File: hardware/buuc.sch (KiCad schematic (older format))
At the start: 12 parts, among them P1 USB_OTG, P2 CONN_01X02, Q1 NDS8434, U1 BOOST_REGULATOR, U2 MCP73842-840I/UN

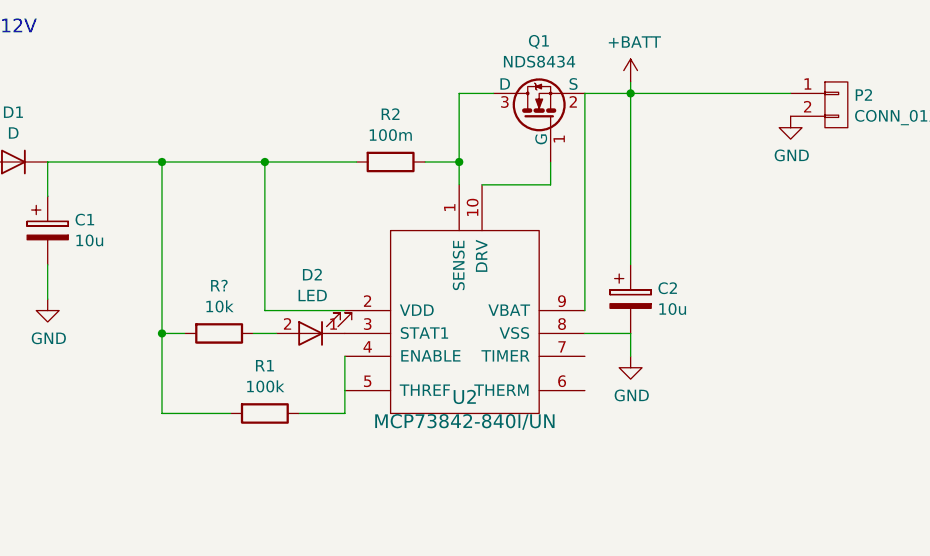
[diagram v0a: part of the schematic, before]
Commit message: Whoops; using the wrong footprint and chip diagram.
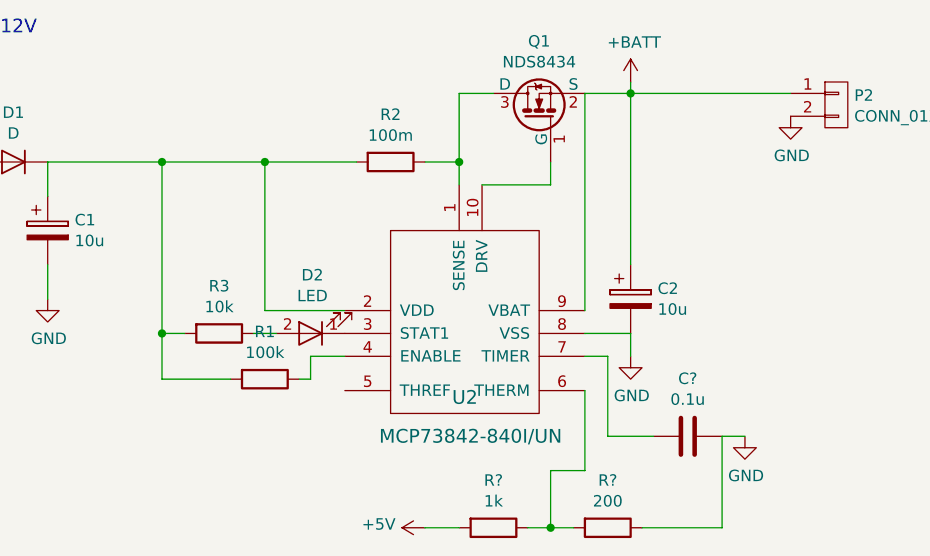
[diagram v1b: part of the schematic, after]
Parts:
- added C?: 0.1u, symbol C
- added R?: 1k, apexelectrix/apex-smd-resistors.pretty:R_0805_HandSoldering, symbol R
- added R?: 200, apexelectrix/apex-smd-resistors.pretty:R_0805_HandSoldering, symbol R
- gave numbers to parts that had none: 1
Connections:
- net +5V: now also R?.2
- net GND: now also C?.1, R?.1
- net at U2.6 (THERM): now also R?.1, R?.2
- net at U2.7 (TIMER): now also C?.2
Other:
- moved on the sheet: R1
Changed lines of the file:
@@
 P 4950 3450
 F 0 "U2" H 4925 2920 60  0000 C CNN
-F 1 "MCP73842-840I/UN" H 4925 2814 60  0000 C CNN
+F 1 "MCP73842-840I/UN" H 4950 2750 60  0000 C CNN
 F 2 "mcous/kicad-lib/footprints/soic.pretty:SOIC8" H 4950 3450 60  0001 C CNN
 F 3 "" H 4950 3450 60  0001 C CNN
@@
 L R R1
 U 1 1 59AF6B9E
-P 4050 4050
-F 0 "R1" V 3843 4050 50  0000 C CNN
-F 1 "100k" V 3934 4050 50  0000 C CNN
-F 2 "apexelectrix/apex-smd-resistors.pretty:R_0805_HandSoldering" V 3980 4050 50  0001 C CNN
-F 3 "" H 4050 4050 50  0000 C CNN
-	1    4050 4050
+P 4050 3900
+F 0 "R1" V 3843 3900 50  0000 C CNN
+F 1 "100k" V 3934 3900 50  0000 C CNN
+F 2 "apexelectrix/apex-smd-resistors.pretty:R_0805_HandSoldering" V 3980 3900 50  0001 C CNN
+F 3 "" H 4050 3900 50  0000 C CNN
+	1    4050 3900
 	0    1    1    0
 $EndComp
@@
 Wire Wire Line
 	3100 3400 3100 3550
-Wire Wire Line
-	3600 2950 3600 4050
 Connection ~ 3600 2950
-Wire Wire Line
-	3600 4050 3900 4050
 Connection ~ 3600 3700
-Wire Wire Line
-	4200 4050 4400 4050
-Wire Wire Line
-	4400 4050 4400 3800
 Wire Wire Line
 	3100 2950 4450 2950
@@
 $EndComp
 $Comp
-L R R?
+L R R3
 U 1 1 59AFA07E
 P 3850 3700
-F 0 "R?" V 3643 3700 50  0000 C CNN
+F 0 "R3" V 3643 3700 50  0000 C CNN
 F 1 "10k" V 3734 3700 50  0000 C CNN
 F 2 "apexelectrix/apex-smd-resistors.pretty:R_0805_HandSoldering" V 3780 3700 50  0001 C CNN
@@
 Wire Wire Line
 	4000 3700 4100 3700
+Wire Wire Line
+	3600 2950 3600 3900
+Wire Wire Line
+	3600 3900 3900 3900
+Wire Wire Line
+	4200 3900 4250 3900
+Wire Wire Line
+	4250 3900 4250 3800
+Wire Wire Line
+	4250 3800 4400 3800
+Wire Wire Line
+	5450 3800 5550 3800
+Wire Wire Line
+	5550 3800 5550 4150
+Wire Wire Line
+	5550 4150 5750 4150
+$Comp
+L C C?
+U 1 1 59AFAA35
+P 5900 4150
+F 0 "C?" V 5648 4150 50  0000 C CNN
+F 1 "0.1u" V 5739 4150 50  0000 C CNN
+F 2 "" H 5938 4000 50  0000 C CNN
+F 3 "" H 5900 4150 50  0000 C CNN
+	1    5900 4150
+	0    1    1    0
+$EndComp
+$Comp
+L GND #PWR?
+U 1 1 59AFAA9C
+P 6150 4150
+F 0 "#PWR?" H 6150 3900 50  0001 C CNN
+F 1 "GND" H 6155 3977 50  0000 C CNN
+F 2 "" H 6150 4150 50  0000 C CNN
+F 3 "" H 6150 4150 50  0000 C CNN
+	1    6150 4150
+	1    0    0    -1
+$EndComp
+Wire Wire Line
+	6050 4150 6150 4150
+$Comp
+L R R?
+U 1 1 59AFAD5C
+P 5050 4550
+F 0 "R?" V 4843 4550 50  0000 C CNN
+F 1 "1k" V 4934 4550 50  0000 C CNN
+F 2 "apexelectrix/apex-smd-resistors.pretty:R_0805_HandSoldering" V 4980 4550 50  0001 C CNN
+F 3 "" H 5050 4550 50  0000 C CNN
+	1    5050 4550
+	0    1    1    0
+$EndComp
+$Comp
+L R R?
+U 1 1 59AFADA7
+P 5550 4550
+F 0 "R?" V 5343 4550 50  0000 C CNN
+F 1 "200" V 5434 4550 50  0000 C CNN
+F 2 "apexelectrix/apex-smd-resistors.pretty:R_0805_HandSoldering" V 5480 4550 50  0001 C CNN
+F 3 "" H 5550 4550 50  0000 C CNN
+	1    5550 4550
+	0    1    1    0
+$EndComp
+Wire Wire Line
+	5700 4550 6050 4550
+Wire Wire Line
+	6050 4550 6050 4150
+Wire Wire Line
+	5450 3950 5450 4300
+Wire Wire Line
+	5450 4300 5300 4300
+Wire Wire Line
+	5300 4300 5300 4550
+Wire Wire Line
+	5200 4550 5400 4550
+Connection ~ 5300 4550
+$Comp
+L +5V #PWR?
+U 1 1 59AFAFDA
+P 4750 4550
+F 0 "#PWR?" H 4750 4400 50  0001 C CNN
+F 1 "+5V" V 4765 4678 50  0000 L CNN
+F 2 "" H 4750 4550 50  0000 C CNN
+F 3 "" H 4750 4550 50  0000 C CNN
+	1    4750 4550
+	0    -1   -1   0
+$EndComp
+Wire Wire Line
+	4750 4550 4900 4550
 $EndSCHEMATC

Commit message: Committing changes from yesterday.
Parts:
- C3: renamed from C?; footprint (none) -> KiCad/Capacitors_SMD.pretty:C_0805_HandSoldering
- U2: footprint mcous/kicad-lib/footprints/soic.pretty:SOIC8 -> adamgreig/agg-kicad/agg.pretty:MSOP-10
- gave numbers to parts that had none: 2
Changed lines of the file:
@@
 F 0 "U2" H 4925 2920 60  0000 C CNN
 F 1 "MCP73842-840I/UN" H 4950 2750 60  0000 C CNN
-F 2 "mcous/kicad-lib/footprints/soic.pretty:SOIC8" H 4950 3450 60  0001 C CNN
+F 2 "adamgreig/agg-kicad/agg.pretty:MSOP-10" H 4950 3450 60  0001 C CNN
 F 3 "" H 4950 3450 60  0001 C CNN
 	1    4950 3450
@@
 	5550 4150 5750 4150
 $Comp
-L C C?
+L C C3
 U 1 1 59AFAA35
 P 5900 4150
-F 0 "C?" V 5648 4150 50  0000 C CNN
+F 0 "C3" V 5648 4150 50  0000 C CNN
 F 1 "0.1u" V 5739 4150 50  0000 C CNN
-F 2 "" H 5938 4000 50  0000 C CNN
+F 2 "KiCad/Capacitors_SMD.pretty:C_0805_HandSoldering" H 5938 4000 50  0001 C CNN
 F 3 "" H 5900 4150 50  0000 C CNN
 	1    5900 4150
@@
 $EndComp
 $Comp
-L GND #PWR?
+L GND #PWR012
 U 1 1 59AFAA9C
 P 6150 4150
-F 0 "#PWR?" H 6150 3900 50  0001 C CNN
+F 0 "#PWR012" H 6150 3900 50  0001 C CNN
 F 1 "GND" H 6155 3977 50  0000 C CNN
 F 2 "" H 6150 4150 50  0000 C CNN
@@
 	6050 4150 6150 4150
 $Comp
-L R R?
+L R R4
 U 1 1 59AFAD5C
 P 5050 4550
-F 0 "R?" V 4843 4550 50  0000 C CNN
+F 0 "R4" V 4843 4550 50  0000 C CNN
 F 1 "1k" V 4934 4550 50  0000 C CNN
 F 2 "apexelectrix/apex-smd-resistors.pretty:R_0805_HandSoldering" V 4980 4550 50  0001 C CNN
@@
 $EndComp
 $Comp
-L R R?
+L R R5
 U 1 1 59AFADA7
 P 5550 4550
-F 0 "R?" V 5343 4550 50  0000 C CNN
+F 0 "R5" V 5343 4550 50  0000 C CNN
 F 1 "200" V 5434 4550 50  0000 C CNN
 F 2 "apexelectrix/apex-smd-resistors.pretty:R_0805_HandSoldering" V 5480 4550 50  0001 C CNN
@@
 Connection ~ 5300 4550
 $Comp
-L +5V #PWR?
+L +5V #PWR013
 U 1 1 59AFAFDA
 P 4750 4550
-F 0 "#PWR?" H 4750 4400 50  0001 C CNN
+F 0 "#PWR013" H 4750 4400 50  0001 C CNN
 F 1 "+5V" V 4765 4678 50  0000 L CNN
 F 2 "" H 4750 4550 50  0000 C CNN

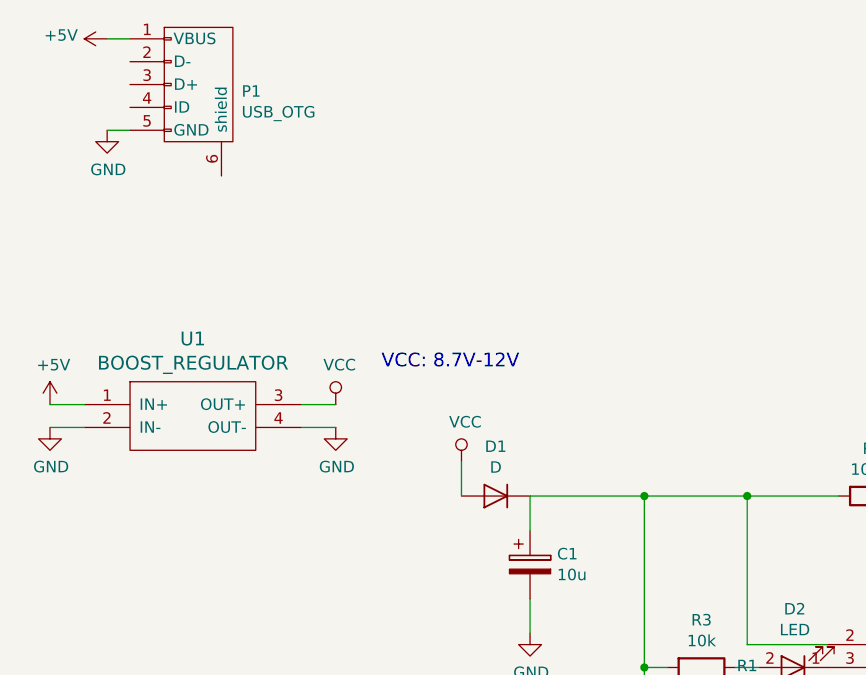
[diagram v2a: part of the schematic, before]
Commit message: Adding MIC2005 current limiting IC; I haven't even soldered everything together, but it's pretty clear this will be necessary.
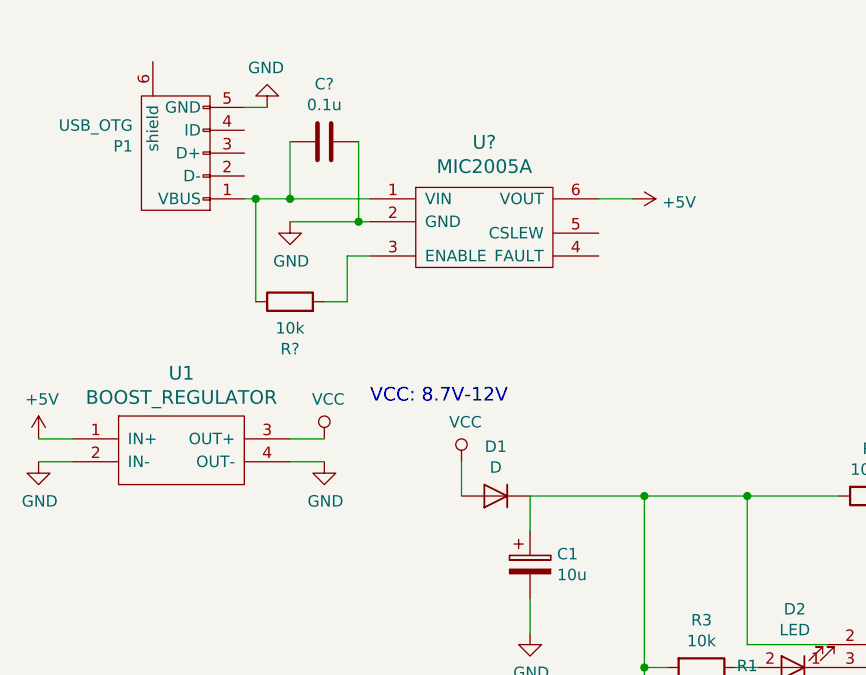
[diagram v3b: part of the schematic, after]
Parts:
- added C?: 0.1u, KiCad/Capacitors_SMD.pretty:C_0805_HandSoldering, symbol C
- added R?: 10k, apexelectrix/apex-smd-resistors.pretty:R_0805_HandSoldering, symbol R
- added U?: MIC2005A, symbol MIC2005A
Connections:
- net +5V: now also U?.6 (VOUT); no longer P1.1 (VBUS)
- net GND: now also C?.1, U?.2 (GND)
- new net: C?.2, P1.1 (VBUS), R?.1, U?.1 (VIN)
- new net: R?.2, U?.3 (ENABLE)
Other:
- moved on the sheet: P1, U1
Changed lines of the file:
@@
 L USB_OTG P1
 U 1 1 59AF531F
-P 1650 1150
-F 0 "P1" V 1680 1338 50  0000 L CNN
-F 1 "USB_OTG" V 1771 1338 50  0000 L CNN
-F 2 "coddingtonbear/coddingtonbear.pretty:MICRO-B_USB-INVERTED" V 1600 1050 50  0001 C CNN
-F 3 "" V 1600 1050 50  0000 C CNN
-	1    1650 1150
-	0    1    1    0
+P 1550 1450
+F 0 "P1" V 1580 1638 50  0000 L CNN
+F 1 "USB_OTG" V 1671 1638 50  0000 L CNN
+F 2 "coddingtonbear/coddingtonbear.pretty:MICRO-B_USB-INVERTED" V 1500 1350 50  0001 C CNN
+F 3 "" V 1500 1350 50  0000 C CNN
+	1    1550 1450
+	0    -1   -1   0
 $EndComp
 $Comp
@@
 L BOOST_REGULATOR U1
 U 1 1 59AF6228
-P 1650 2600
-F 0 "U1" H 1625 2937 60  0000 C CNN
-F 1 "BOOST_REGULATOR" H 1625 2831 60  0000 C CNN
-F 2 "coddingtonbear/coddingtonbear.pretty:BOOST_REGULATOR" H 1650 2600 60  0001 C CNN
-F 3 "" H 1650 2600 60  0001 C CNN
-	1    1650 2600
+P 1600 2750
+F 0 "U1" H 1575 3087 60  0000 C CNN
+F 1 "BOOST_REGULATOR" H 1575 2981 60  0000 C CNN
+F 2 "coddingtonbear/coddingtonbear.pretty:BOOST_REGULATOR" H 1600 2750 60  0001 C CNN
+F 3 "" H 1600 2750 60  0001 C CNN
+	1    1600 2750
 	1    0    0    -1
 $EndComp
@@
 L +5V #PWR01
 U 1 1 59AF62AD
-P 1250 950
-F 0 "#PWR01" H 1250 800 50  0001 C CNN
-F 1 "+5V" V 1265 1078 50  0000 L CNN
-F 2 "" H 1250 950 50  0000 C CNN
-F 3 "" H 1250 950 50  0000 C CNN
-	1    1250 950
-	0    -1   -1   0
+P 3550 1650
+F 0 "#PWR01" H 3550 1500 50  0001 C CNN
+F 1 "+5V" V 3565 1778 50  0000 L CNN
+F 2 "" H 3550 1650 50  0000 C CNN
+F 3 "" H 3550 1650 50  0000 C CNN
+	1    3550 1650
+	0    1    1    0
 $EndComp
 $Comp
 L +5V #PWR02
 U 1 1 59AF62D9
-P 1000 2550
-F 0 "#PWR02" H 1000 2400 50  0001 C CNN
-F 1 "+5V" H 1015 2723 50  0000 C CNN
-F 2 "" H 1000 2550 50  0000 C CNN
-F 3 "" H 1000 2550 50  0000 C CNN
-	1    1000 2550
+P 950 2700
+F 0 "#PWR02" H 950 2550 50  0001 C CNN
+F 1 "+5V" H 965 2873 50  0000 C CNN
+F 2 "" H 950 2700 50  0000 C CNN
+F 3 "" H 950 2700 50  0000 C CNN
+	1    950  2700
 	1    0    0    -1
 $EndComp
@@
 L GND #PWR03
 U 1 1 59AF6327
-P 1000 2650
-F 0 "#PWR03" H 1000 2400 50  0001 C CNN
-F 1 "GND" H 1005 2477 50  0000 C CNN
-F 2 "" H 1000 2650 50  0000 C CNN
-F 3 "" H 1000 2650 50  0000 C CNN
-	1    1000 2650
+P 950 2800
+F 0 "#PWR03" H 950 2550 50  0001 C CNN
+F 1 "GND" H 955 2627 50  0000 C CNN
+F 2 "" H 950 2800 50  0000 C CNN
+F 3 "" H 950 2800 50  0000 C CNN
+	1    950  2800
 	1    0    0    -1
 $EndComp
@@
 L GND #PWR04
 U 1 1 59AF634E
-P 2250 2650
-F 0 "#PWR04" H 2250 2400 50  0001 C CNN
-F 1 "GND" H 2255 2477 50  0000 C CNN
-F 2 "" H 2250 2650 50  0000 C CNN
-F 3 "" H 2250 2650 50  0000 C CNN
-	1    2250 2650
+P 2200 2800
+F 0 "#PWR04" H 2200 2550 50  0001 C CNN
+F 1 "GND" H 2205 2627 50  0000 C CNN
+F 2 "" H 2200 2800 50  0000 C CNN
+F 3 "" H 2200 2800 50  0000 C CNN
+	1    2200 2800
 	1    0    0    -1
 $EndComp
@@
 L GND #PWR05
 U 1 1 59AF6362
-P 1250 1350
-F 0 "#PWR05" H 1250 1100 50  0001 C CNN
-F 1 "GND" H 1255 1177 50  0000 C CNN
-F 2 "" H 1250 1350 50  0000 C CNN
-F 3 "" H 1250 1350 50  0000 C CNN
-	1    1250 1350
-	1    0    0    -1
-$EndComp
-Wire Wire Line
-	1250 950  1350 950
-Wire Wire Line
-	1250 1350 1350 1350
-Wire Wire Line
-	2100 2650 2250 2650
-Wire Wire Line
-	1000 2650 1150 2650
-Wire Wire Line
-	1000 2550 1150 2550
+P 1950 1250
+F 0 "#PWR05" H 1950 1000 50  0001 C CNN
+F 1 "GND" H 1955 1077 50  0000 C CNN
+F 2 "" H 1950 1250 50  0000 C CNN
+F 3 "" H 1950 1250 50  0000 C CNN
+	1    1950 1250
+	-1   0    0    1
+$EndComp
+Wire Wire Line
+	1850 1650 2400 1650
+Wire Wire Line
+	1950 1250 1850 1250
+Wire Wire Line
+	2050 2800 2200 2800
+Wire Wire Line
+	950  2800 1100 2800
+Wire Wire Line
+	950  2700 1100 2700
 $Comp
 L VCC #PWR06
 U 1 1 59AF63A7
-P 2250 2550
-F 0 "#PWR06" H 2250 2400 50  0001 C CNN
-F 1 "VCC" H 2267 2723 50  0000 C CNN
-F 2 "" H 2250 2550 50  0000 C CNN
-F 3 "" H 2250 2550 50  0000 C CNN
-	1    2250 2550
-	1    0    0    -1
-$EndComp
-Wire Wire Line
-	2100 2550 2250 2550
+P 2200 2700
+F 0 "#PWR06" H 2200 2550 50  0001 C CNN
+F 1 "VCC" H 2217 2873 50  0000 C CNN
+F 2 "" H 2200 2700 50  0000 C CNN
+F 3 "" H 2200 2700 50  0000 C CNN
+	1    2200 2700
+	1    0    0    -1
+$EndComp
+Wire Wire Line
+	2050 2700 2200 2700
 $Comp
 L VCC #PWR07
@@
 	1    0    0    -1
 $EndComp
-Text Notes 2450 2400 0    60   ~ 0
+Text Notes 2400 2550 0    60   ~ 0
 VCC: 8.7V-12V
 $Comp
@@
 Wire Wire Line
 	4750 4550 4900 4550
+$Comp
+L MIC2005A U?
+U 1 1 59BADA49
+P 2900 1750
+F 0 "U?" H 2900 2097 60  0000 C CNN
+F 1 "MIC2005A" H 2900 1991 60  0000 C CNN
+F 2 "" H 2900 1750 60  0001 C CNN
+F 3 "" H 2900 1750 60  0001 C CNN
+	1    2900 1750
+	1    0    0    -1
+$EndComp
+Wire Wire Line
+	3550 1650 3400 1650
+$Comp
+L GND #PWR?
+U 1 1 59BADB64
+P 2050 1750
+F 0 "#PWR?" H 2050 1500 50  0001 C CNN
+F 1 "GND" H 2055 1577 50  0000 C CNN
+F 2 "" H 2050 1750 50  0000 C CNN
+F 3 "" H 2050 1750 50  0000 C CNN
+	1    2050 1750
+	1    0    0    -1
+$EndComp
+Wire Wire Line
+	2400 1750 2050 1750
+$Comp
+L R R?
+U 1 1 59BADC60
+P 2050 2100
+F 0 "R?" V 1843 2100 50  0000 C CNN
+F 1 "10k" V 1934 2100 50  0000 C CNN
+F 2 "apexelectrix/apex-smd-resistors.pretty:R_0805_HandSoldering" V 1980 2100 50  0001 C CNN
+F 3 "" H 2050 2100 50  0000 C CNN
+	1    2050 2100
+	0    -1   -1   0
+$EndComp
+Wire Wire Line
+	2200 2100 2300 2100
+Wire Wire Line
+	2300 2100 2300 1900
+Wire Wire Line
+	2300 1900 2400 1900
+Wire Wire Line
+	1900 2100 1900 1650
+Connection ~ 1900 1650
+$Comp
+L C C?
+U 1 1 59BAE16D
+P 2200 1400
+F 0 "C?" V 1948 1400 50  0000 C CNN
+F 1 "0.1u" V 2039 1400 50  0000 C CNN
+F 2 "KiCad/Capacitors_SMD.pretty:C_0805_HandSoldering" H 2238 1250 50  0001 C CNN
+F 3 "" H 2200 1400 50  0000 C CNN
+	1    2200 1400
+	0    1    1    0
+$EndComp
+Wire Wire Line
+	2350 1400 2350 1750
+Connection ~ 2350 1750
+Wire Wire Line
+	2050 1400 2050 1650
+Connection ~ 2050 1650
 $EndSCHEMATC
